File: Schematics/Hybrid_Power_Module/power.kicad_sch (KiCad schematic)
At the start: 97 parts, among them J1 ScrewSwitch, J2 Battery, J3 ScrewSwitch, J4 GSE, J7 Stack Male Edge Connector, Q1 AO4447A, Q2 SI2305CDS, Q3 DMN6040SSD-13, U1 TPS61175PWPR, U10 LM66100DCKR, U11 LM66100DCKR, U12 AMS1117-3.3, U2 LM74700QDBVRQ1, U3 LM74700QDBVRQ1, U4 ACS37041KLHBLT-010B3, U5 ACS37041KLHBLT-010B5, U6 INA187A, U7 LMR51430XDDCR, U8 LMR51430XDDCR, U9 LM66100DCKR

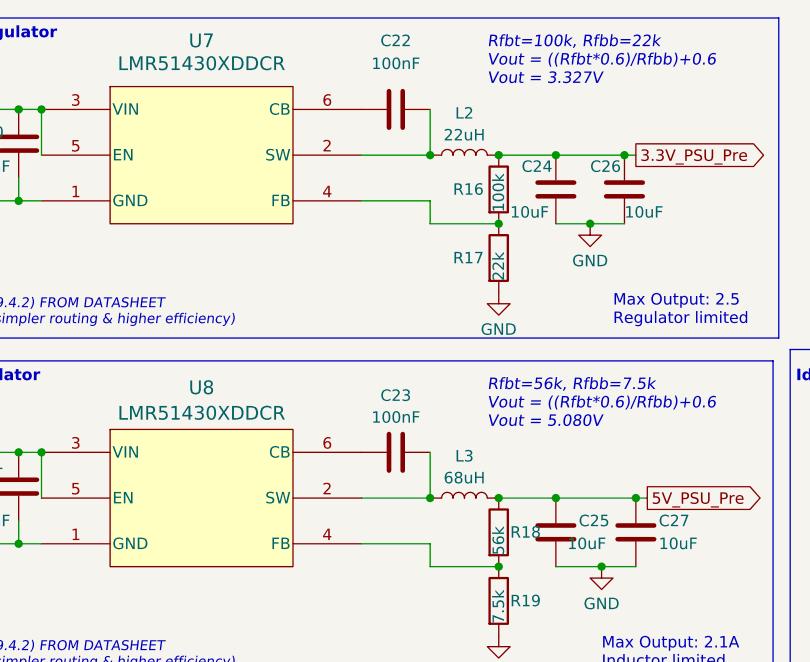
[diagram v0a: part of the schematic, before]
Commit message: using copper poor for 5v and 3.3v buck sw
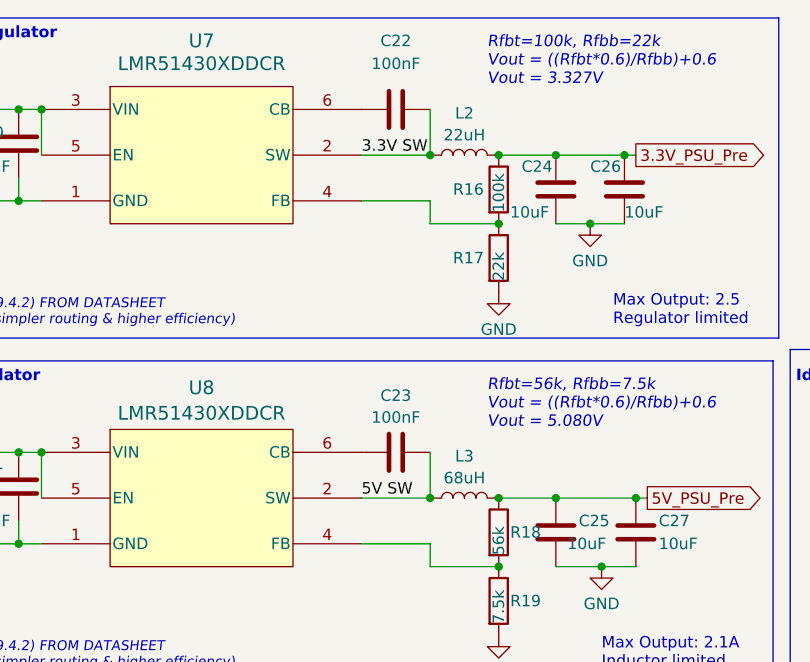
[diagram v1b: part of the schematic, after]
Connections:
- net 5V SW: now reaches C23.1, L3.1, U8.2 (SW)
- net 3.3V SW: now reaches C22.2, L2.2, U7.2 (SW)
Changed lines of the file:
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@@
+		)
+	)
+	(label "5V SW"
+		(at 274.32 67.31 0)
+		(fields_autoplaced yes)
+		(effects
+			(font
+				(size 1.27 1.27)
+			)
+			(justify left bottom)
 		)
 	)
@@
 		(fields_autoplaced yes)
 		(effects
+			(font
+				(size 1.27 1.27)
+			)
+			(justify left bottom)
+		)
+	)
+	(label "3.3V SW"
+		(at 274.32 29.21 0)
+		(fields_autoplaced yes)
+		(effects
